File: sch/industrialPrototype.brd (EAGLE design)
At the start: 160 x 100 mm, 12 parts, among them IC1 LD1117V33C, U1 PIC16F1825-I/SL

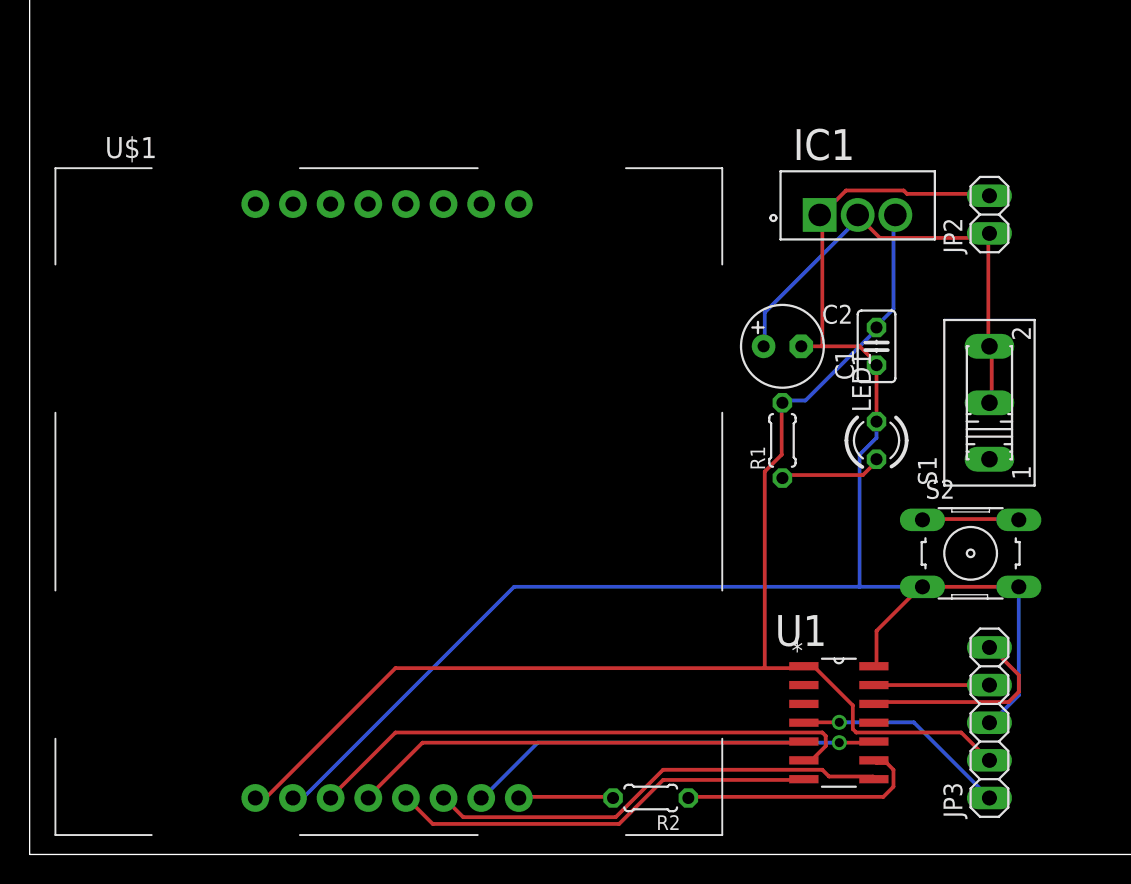
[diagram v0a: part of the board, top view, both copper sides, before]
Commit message: Added the Temperature Sensor Socket
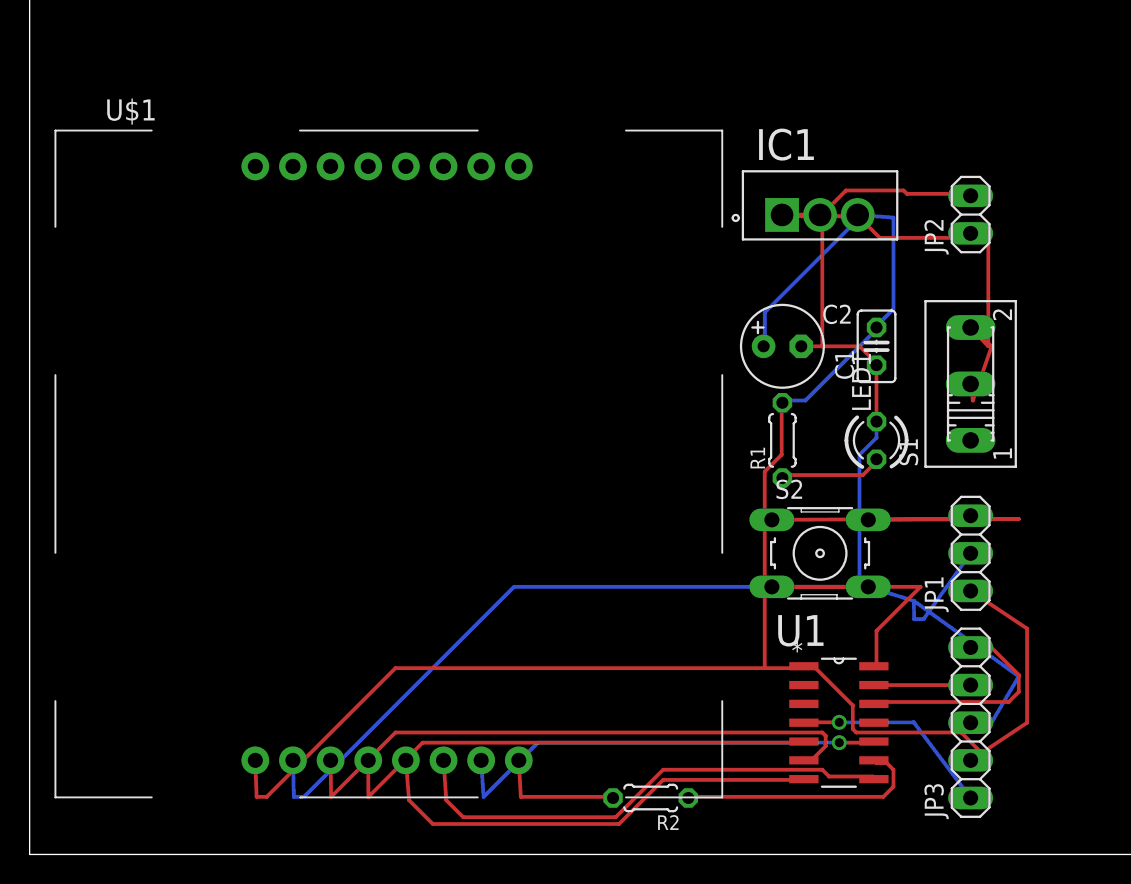
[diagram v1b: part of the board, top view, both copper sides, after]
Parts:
- added JP1: (no value), pinhead:1X03
- moved S2 10.2 mm to (53.3, 20.3)
- moved U$1 2.54 mm to (15.2, 6.35)
- moved IC1 2.54 mm to (55.9, 44.5)
- moved S1 1.80 mm to (63.5, 31.8)
- moved JP2 1.27 mm to (63.5, 43.2)
- moved JP3 1.27 mm to (63.5, 8.89)
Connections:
- new net 1WIRE_DS18B20: JP1.3, U1.11
- net 3V3: now also JP1.1
- net GND: now also JP1.2
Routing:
- net GND: track 114.1 -> 142.4 mm
- net 3V3: track 91.8 -> 113.0 mm
- net !MCLK!: track 6.57 -> 26.8 mm
- net VBAT: track 33.2 -> 44.6 mm
- net DN(MOSI): track 31.2 -> 33.7 mm
- net D/C: track 28.8 -> 31.2 mm
- net !RST!: track 31.0 -> 33.4 mm
- net !SCE!: track 37.9 -> 40.3 mm
- net LED: track 6.42 -> 8.73 mm
- net SCLK: track 28.1 -> 30.4 mm
- net ICSPDAT: track 7.80 -> 6.53 mm
- net ICSPCLK: track 14.0 -> 15.3 mm
- net !MCLR!: track 14.6 -> 13.8 mm

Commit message: Final Version of the Schematic and Board
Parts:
- removed U$1: NOKIA5110, CustomLib:NOKIA5110
- added NOKIA5110: NOKIA5110, CustomLib:NOKIA5110
- moved LED1 20.5 mm to (64.8, 47.0)
- moved S2 9.16 mm to (61.0, 25.4)
- moved JP3 7.18 mm to (68.6, 14.0)
- moved JP1 7.18 mm to (68.6, 25.4), turned to 270 degrees
- moved C1 6.35 mm to (53.3, 29.2), turned to 0 degrees
- moved JP2 5.24 mm to (68.6, 41.9), turned to 270 degrees
- moved R1 5.08 mm to (50.8, 22.9)
- moved U1 4.58 mm to (58.4, 11.4)
- moved R2 4.02 mm to (38.1, 2.54)
- moved IC1 3.59 mm to (58.4, 47.0)
- moved C2 2.54 mm to (53.3, 34.3), turned to 90 degrees
- moved S1 2.54 mm to (63.5, 34.3), turned to 0 degrees
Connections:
- net !RST!: now also NOKIA5110.B4; no longer U$1.B4
- net !SCE!: now also NOKIA5110.B3; no longer U$1.B3
- net 3V3: now also NOKIA5110.B1; no longer U$1.B1
- net D/C: now also NOKIA5110.B5; no longer U$1.B5
- net DN(MOSI): now also NOKIA5110.B6; no longer U$1.B6
- net GND: now also NOKIA5110.B2; no longer U$1.B2
- net LED: now also NOKIA5110.B8; no longer U$1.B8
- net SCLK: now also NOKIA5110.B7; no longer U$1.B7
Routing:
- net N$1: track 6.97 -> 31.2 mm
- net !MCLK!: track 26.8 -> 6.50 mm
- net GND: track 142.4 -> 124.2 mm
- net 1WIRE_DS18B20: track 0.00 -> 18.1 mm
- net VBAT: track 44.6 -> 38.6 mm
- net N$3: track 16.9 -> 22.8 mm
- net LED: track 8.73 -> 3.87 mm
- net !SCE!: track 40.3 -> 35.5 mm, vias 0 -> 1
- net SCLK: track 30.4 -> 33.8 mm, vias 1 -> 0
- net !RST!: track 33.4 -> 36.4 mm
- net ICSPDAT: track 6.53 -> 8.97 mm
- net DN(MOSI): track 33.7 -> 31.6 mm, vias 0 -> 1
- net D/C: track 31.2 -> 29.2 mm, vias 0 -> 1
- net 3V3: track 113.0 -> 113.8 mm
- net ICSPCLK: track 15.3 -> 14.5 mm
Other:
- board size 160 x 100 mm -> 74.9 x 53 mm
